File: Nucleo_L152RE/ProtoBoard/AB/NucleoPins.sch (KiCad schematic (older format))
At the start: 2 parts, among them U2 Nucleo-L152RE-CN7, U3 Nucleo-L152RE-CN10

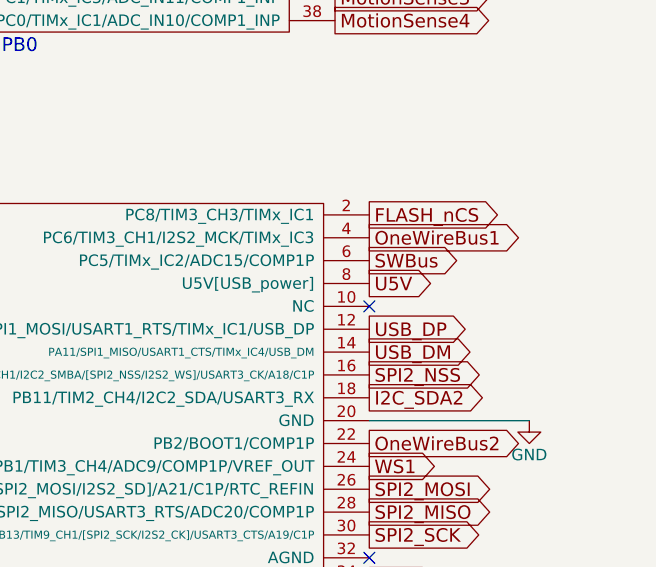
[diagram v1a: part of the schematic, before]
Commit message: Final draft with all traces and artwork in place.
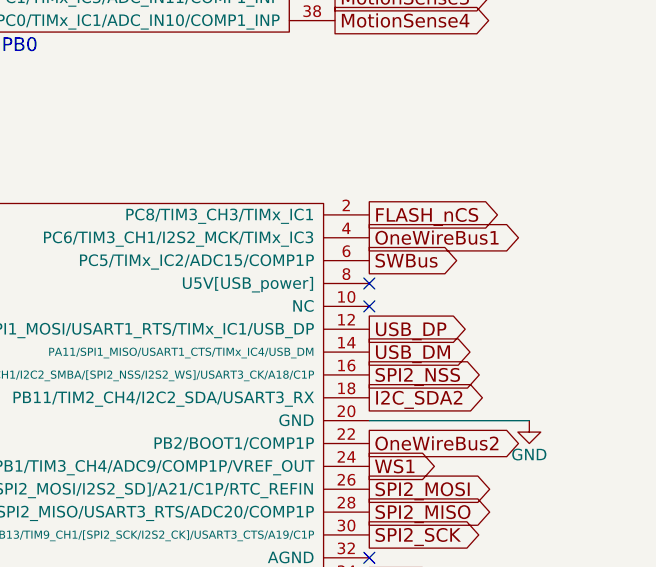
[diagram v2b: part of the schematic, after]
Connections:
- net U5V: no longer names the net of U3.8 (U5V[USB_power])
- no-connect marks 13 -> 14
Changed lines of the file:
@@
 Sheet 3 5
 Title "Expansion Board For STM32 Nucleo-L152RE"
-Date "Saturday, May 23, 2015"
-Rev "AB - Draft"
+Date "Sunday, May 31, 2015"
+Rev "AB - Final Draft"
 Comp "Open Source Hardware"
 Comment1 "MIT License"
@@
 Not 5V Tolerant: PC3, PA3, PA4, PA5, PB0
 $Comp
-L GND #PWR029
+L GND #PWR028
 U 1 1 555A9D07
 P 8200 2150
-F 0 "#PWR029" H 8200 1900 50  0001 C CNN
+F 0 "#PWR028" H 8200 1900 50  0001 C CNN
 F 1 "GND" H 8200 2000 50  0000 C CNN
 F 2 "" H 8200 2150 60  0000 C CNN
@@
 $EndComp
 $Comp
-L GND #PWR030
+L GND #PWR029
 U 1 1 555A9D0D
 P 8150 1550
-F 0 "#PWR030" H 8150 1300 50  0001 C CNN
+F 0 "#PWR029" H 8150 1300 50  0001 C CNN
 F 1 "GND" H 8150 1400 50  0000 C CNN
 F 2 "" H 8150 1550 60  0000 C CNN
@@
 NoConn ~ 2950 1550
 $Comp
-L GND #PWR031
+L GND #PWR030
 U 1 1 555A9D1E
 P 8550 4800
-F 0 "#PWR031" H 8550 4550 50  0001 C CNN
+F 0 "#PWR030" H 8550 4550 50  0001 C CNN
 F 1 "GND" H 8550 4650 50  0000 C CNN
 F 2 "" H 8550 4800 60  0000 C CNN
@@
 $EndComp
 $Comp
-L GND #PWR032
+L GND #PWR031
 U 1 1 555A9D24
 P 1800 4200
-F 0 "#PWR032" H 1800 3950 50  0001 C CNN
+F 0 "#PWR031" H 1800 3950 50  0001 C CNN
 F 1 "GND" H 1800 4050 50  0000 C CNN
 F 2 "" H 1800 4200 60  0000 C CNN
@@
 $EndComp
 $Comp
-L GND #PWR033
+L GND #PWR032
 U 1 1 555A9D2A
 P 2150 2150
-F 0 "#PWR033" H 2150 1900 50  0001 C CNN
+F 0 "#PWR032" H 2150 1900 50  0001 C CNN
 F 1 "GND" H 2150 2000 50  0000 C CNN
 F 2 "" H 2150 2150 60  0000 C CNN
@@
 NoConn ~ 7850 5400
 $Comp
-L +15V #PWR034
+L +15V #PWR033
 U 1 1 555A9D36
 P 8450 2350
-F 0 "#PWR034" H 8450 2200 50  0001 C CNN
+F 0 "#PWR033" H 8450 2200 50  0001 C CNN
 F 1 "+15V" H 8450 2490 50  0000 C CNN
 F 2 "" H 8450 2350 60  0000 C CNN
@@
 $EndComp
 $Comp
-L +3V3 #PWR035
+L +3V3 #PWR034
 U 1 1 555A9D3D
 P 2200 1450
-F 0 "#PWR035" H 2200 1300 50  0001 C CNN
+F 0 "#PWR034" H 2200 1300 50  0001 C CNN
 F 1 "+3V3" H 2200 1590 50  0000 C CNN
 F 2 "" H 2200 1450 60  0000 C CNN
@@
 Text GLabel 7850 4100 2    59   Output ~ 0
 SWBus
-Text GLabel 7850 4200 2    59   Output ~ 0
-U5V
 Text GLabel 7850 4400 2    59   Output ~ 0
 USB_DP
@@
 Wire Wire Line
 	7850 4800 8550 4800
+NoConn ~ 7850 4200
 $EndSCHEMATC
